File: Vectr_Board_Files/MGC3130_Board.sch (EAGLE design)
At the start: 108 parts, among them U101 MCP1755S, U102 MGC3130, U201 74HCT595BQ,115, U202 74HCT595BQ,115, U203 74HCT595BQ,115

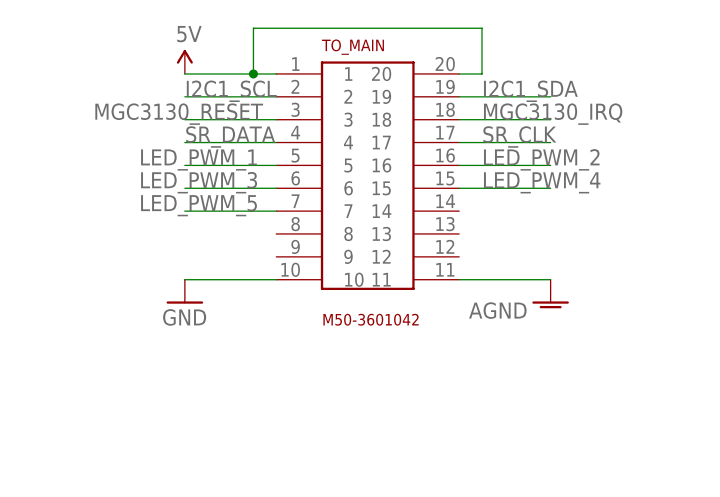
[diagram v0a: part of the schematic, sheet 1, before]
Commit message: Changing connectors
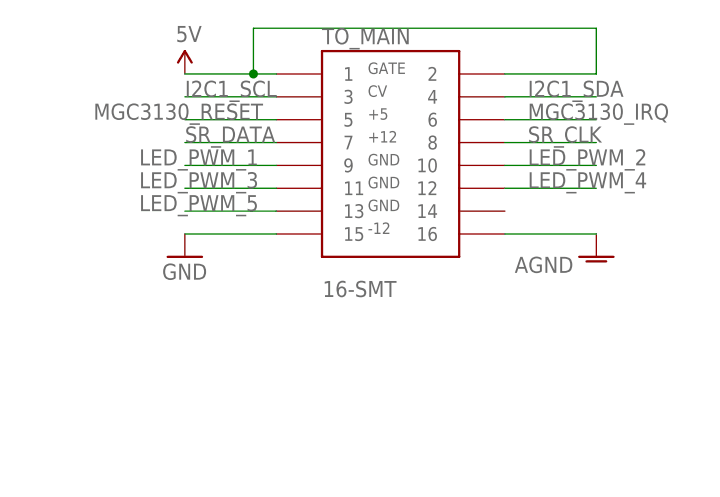
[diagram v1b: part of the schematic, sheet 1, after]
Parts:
- TO_MAIN: value M50-3601042 -> 16-SMT; device HackMe:M50-3601042 -> HackMe:16-SMT
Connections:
- net 5V: now also TO_MAIN.2; no longer TO_MAIN.20
- net AGND: now also TO_MAIN.16; no longer TO_MAIN.11
- net GND: now also TO_MAIN.15; no longer TO_MAIN.10
- net I2C1_SCL: now also TO_MAIN.3; no longer TO_MAIN.2
- net I2C1_SDA: now also TO_MAIN.4; no longer TO_MAIN.19
- net LED_PWM_1: now also TO_MAIN.9; no longer TO_MAIN.5
- net LED_PWM_2: now also TO_MAIN.10; no longer TO_MAIN.16
- net LED_PWM_3: now also TO_MAIN.11; no longer TO_MAIN.6
- net LED_PWM_4: now also TO_MAIN.12; no longer TO_MAIN.15
- net LED_PWM_5: now also TO_MAIN.13; no longer TO_MAIN.7
- net MGC3130_IRQ: now also TO_MAIN.6; no longer TO_MAIN.18
- net MGC3130_RESET: now also TO_MAIN.5; no longer TO_MAIN.3
- net SR_CLK: now also TO_MAIN.8; no longer TO_MAIN.17
- net SR_DATA: now also TO_MAIN.7; no longer TO_MAIN.4
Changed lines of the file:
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@@
 <part name="GND2" library="supply1" deviceset="GND" device=""/>
 <part name="AGND3" library="supply1" deviceset="AGND" device=""/>
-<part name="TO_MAIN" library="HackMe" deviceset="M50-3601042" device=""/>
 <part name="USB_BRIDGE" library="HackMe" deviceset="1X6_2MM_HEADER" device=""/>
+<part name="TO_MAIN" library="HackMe" deviceset="16-SMT" device=""/>
 </parts>
 <sheets>
@@
 <instance part="SUPPLY33" gate="G$1" x="-78.74" y="88.9"/>
 <instance part="SUPPLY38" gate="G$1" x="55.88" y="91.44"/>
-<instance part="GND34" gate="1" x="55.88" y="66.04"/>
-<instance part="AGND14" gate="VR1" x="96.52" y="66.04" smashed="yes">
-<attribute name="VALUE" x="93.98" y="66.04" size="1.778" layer="96" rot="R180"/>
+<instance part="GND34" gate="1" x="55.88" y="71.12"/>
+<instance part="AGND14" gate="VR1" x="101.6" y="71.12" smashed="yes">
+<attribute name="VALUE" x="99.06" y="71.12" size="1.778" layer="96" rot="R180"/>
 </instance>
 <instance part="AGND17" gate="VR1" x="-7.62" y="-45.72" smashed="yes">
@@
 <attribute name="VALUE" x="20.32" y="-20.32" size="1.778" layer="96" rot="R180"/>
 </instance>
-<instance part="TO_MAIN" gate="G$1" x="73.66" y="76.2"/>
 <instance part="USB_BRIDGE" gate="G$1" x="-71.12" y="-73.66"/>
+<instance part="TO_MAIN" gate="G$1" x="76.2" y="83.82"/>
 </instances>
 <busses>
@@
 <segment>
 <pinref part="GND34" gate="1" pin="GND"/>
-<wire x1="66.04" y1="68.58" x2="55.88" y2="68.58" width="0.1524" layer="91"/>
-<pinref part="TO_MAIN" gate="G$1" pin="10"/>
+<wire x1="66.04" y1="73.66" x2="55.88" y2="73.66" width="0.1524" layer="91"/>
+<pinref part="TO_MAIN" gate="G$1" pin="15"/>
 </segment>
 <segment>
@@
 </segment>
 <segment>
-<wire x1="86.36" y1="86.36" x2="96.52" y2="86.36" width="0.1524" layer="91"/>
-<label x="88.9" y="86.36" size="1.778" layer="95"/>
-<pinref part="TO_MAIN" gate="G$1" pin="18"/>
+<wire x1="91.44" y1="86.36" x2="101.6" y2="86.36" width="0.1524" layer="91"/>
+<label x="93.98" y="86.36" size="1.778" layer="95"/>
+<pinref part="TO_MAIN" gate="G$1" pin="6"/>
 </segment>
 <segment>
@@
 </segment>
 <segment>
-<wire x1="86.36" y1="88.9" x2="96.52" y2="88.9" width="0.1524" layer="91"/>
-<label x="88.9" y="88.9" size="1.778" layer="95"/>
-<pinref part="TO_MAIN" gate="G$1" pin="19"/>
+<wire x1="91.44" y1="88.9" x2="101.6" y2="88.9" width="0.1524" layer="91"/>
+<label x="93.98" y="88.9" size="1.778" layer="95"/>
+<pinref part="TO_MAIN" gate="G$1" pin="4"/>
 </segment>
 <segment>
@@
 <wire x1="66.04" y1="88.9" x2="55.88" y2="88.9" width="0.1524" layer="91"/>
 <label x="55.88" y="88.9" size="1.778" layer="95"/>
-<pinref part="TO_MAIN" gate="G$1" pin="2"/>
+<pinref part="TO_MAIN" gate="G$1" pin="3"/>
 </segment>
 <segment>
@@
 <wire x1="66.04" y1="86.36" x2="55.88" y2="86.36" width="0.1524" layer="91"/>
 <label x="45.72" y="86.36" size="1.778" layer="95"/>
-<pinref part="TO_MAIN" gate="G$1" pin="3"/>
+<pinref part="TO_MAIN" gate="G$1" pin="5"/>
 </segment>
 <segment>
@@
 <wire x1="63.5" y1="91.44" x2="63.5" y2="96.52" width="0.1524" layer="91"/>
 <junction x="63.5" y="91.44"/>
-<wire x1="63.5" y1="96.52" x2="88.9" y2="96.52" width="0.1524" layer="91"/>
-<wire x1="88.9" y1="96.52" x2="88.9" y2="91.44" width="0.1524" layer="91"/>
-<wire x1="88.9" y1="91.44" x2="86.36" y2="91.44" width="0.1524" layer="91"/>
+<wire x1="63.5" y1="96.52" x2="101.6" y2="96.52" width="0.1524" layer="91"/>
+<wire x1="101.6" y1="96.52" x2="101.6" y2="91.44" width="0.1524" layer="91"/>
+<wire x1="101.6" y1="91.44" x2="91.44" y2="91.44" width="0.1524" layer="91"/>
 <pinref part="TO_MAIN" gate="G$1" pin="1"/>
-<pinref part="TO_MAIN" gate="G$1" pin="20"/>
+<pinref part="TO_MAIN" gate="G$1" pin="2"/>
 </segment>
 </net>
@@
 <segment>
 <pinref part="AGND14" gate="VR1" pin="AGND"/>
-<wire x1="86.36" y1="68.58" x2="96.52" y2="68.58" width="0.1524" layer="91"/>
-<pinref part="TO_MAIN" gate="G$1" pin="11"/>
+<wire x1="91.44" y1="73.66" x2="101.6" y2="73.66" width="0.1524" layer="91"/>
+<pinref part="TO_MAIN" gate="G$1" pin="16"/>
 </segment>
 <segment>
@@
 <wire x1="66.04" y1="83.82" x2="55.88" y2="83.82" width="0.1524" layer="91"/>
 <label x="55.88" y="83.82" size="1.778" layer="95"/>
-<pinref part="TO_MAIN" gate="G$1" pin="4"/>
+<pinref part="TO_MAIN" gate="G$1" pin="7"/>
 </segment>
 </net>
 <net name="SR_CLK" class="0">
 <segment>
-<wire x1="86.36" y1="83.82" x2="96.52" y2="83.82" width="0.1524" layer="91"/>
-<label x="88.9" y="83.82" size="1.778" layer="95"/>
-<pinref part="TO_MAIN" gate="G$1" pin="17"/>
+<wire x1="91.44" y1="83.82" x2="101.6" y2="83.82" width="0.1524" layer="91"/>
+<label x="93.98" y="83.82" size="1.778" layer="95"/>
+<pinref part="TO_MAIN" gate="G$1" pin="8"/>
 </segment>
 </net>
@@
 <wire x1="66.04" y1="81.28" x2="55.88" y2="81.28" width="0.1524" layer="91"/>
 <label x="50.8" y="81.28" size="1.778" layer="95"/>
-<pinref part="TO_MAIN" gate="G$1" pin="5"/>
+<pinref part="TO_MAIN" gate="G$1" pin="9"/>
 </segment>
 </net>
 <net name="LED_PWM_2" class="0">
 <segment>
-<wire x1="86.36" y1="81.28" x2="96.52" y2="81.28" width="0.1524" layer="91"/>
-<label x="88.9" y="81.28" size="1.778" layer="95"/>
-<pinref part="TO_MAIN" gate="G$1" pin="16"/>
+<wire x1="91.44" y1="81.28" x2="101.6" y2="81.28" width="0.1524" layer="91"/>
+<label x="93.98" y="81.28" size="1.778" layer="95"/>
+<pinref part="TO_MAIN" gate="G$1" pin="10"/>
 </segment>
 </net>
@@
 <wire x1="66.04" y1="78.74" x2="55.88" y2="78.74" width="0.1524" layer="91"/>
 <label x="50.8" y="78.74" size="1.778" layer="95"/>
-<pinref part="TO_MAIN" gate="G$1" pin="6"/>
+<pinref part="TO_MAIN" gate="G$1" pin="11"/>
 </segment>
 </net>
 <net name="LED_PWM_4" class="0">
 <segment>
-<wire x1="86.36" y1="78.74" x2="96.52" y2="78.74" width="0.1524" layer="91"/>
-<label x="88.9" y="78.74" size="1.778" layer="95"/>
-<pinref part="TO_MAIN" gate="G$1" pin="15"/>
+<wire x1="91.44" y1="78.74" x2="101.6" y2="78.74" width="0.1524" layer="91"/>
+<label x="93.98" y="78.74" size="1.778" layer="95"/>
+<pinref part="TO_MAIN" gate="G$1" pin="12"/>
 </segment>
 </net>
@@
 <wire x1="66.04" y1="76.2" x2="55.88" y2="76.2" width="0.1524" layer="91"/>
 <label x="50.8" y="76.2" size="1.778" layer="95"/>
-<pinref part="TO_MAIN" gate="G$1" pin="7"/>
-</segment>
-</net>
+<pinref part="TO_MAIN" gate="G$1" pin="13"/>
+</segment>
+</net>

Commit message: Correcting the board files to match original production Vectr
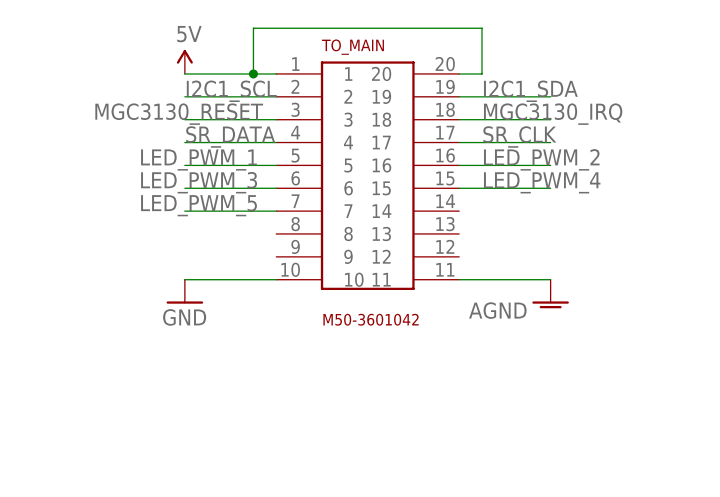
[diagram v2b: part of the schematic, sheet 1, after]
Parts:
- TO_MAIN: value 16-SMT -> M50-3601042; device HackMe:16-SMT -> HackMe:M50-3601042
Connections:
- net 5V: now also TO_MAIN.20; no longer TO_MAIN.2
- net AGND: now also TO_MAIN.11; no longer TO_MAIN.16
- net GND: now also TO_MAIN.10; no longer TO_MAIN.15
- net I2C1_SCL: now also TO_MAIN.2; no longer TO_MAIN.3
- net I2C1_SDA: now also TO_MAIN.19; no longer TO_MAIN.4
- net LED_PWM_1: now also TO_MAIN.5; no longer TO_MAIN.9
- net LED_PWM_2: now also TO_MAIN.16; no longer TO_MAIN.10
- net LED_PWM_3: now also TO_MAIN.6; no longer TO_MAIN.11
- net LED_PWM_4: now also TO_MAIN.15; no longer TO_MAIN.12
- net LED_PWM_5: now also TO_MAIN.7; no longer TO_MAIN.13
- net MGC3130_IRQ: now also TO_MAIN.18; no longer TO_MAIN.6
- net MGC3130_RESET: now also TO_MAIN.3; no longer TO_MAIN.5
- net SR_CLK: now also TO_MAIN.17; no longer TO_MAIN.8
- net SR_DATA: now also TO_MAIN.4; no longer TO_MAIN.7
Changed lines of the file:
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@@
 <part name="GND2" library="supply1" deviceset="GND" device=""/>
 <part name="AGND3" library="supply1" deviceset="AGND" device=""/>
+<part name="TO_MAIN" library="HackMe" deviceset="M50-3601042" device=""/>
 <part name="USB_BRIDGE" library="HackMe" deviceset="1X6_2MM_HEADER" device=""/>
-<part name="TO_MAIN" library="HackMe" deviceset="16-SMT" device=""/>
 </parts>
 <sheets>
@@
 <instance part="SUPPLY33" gate="G$1" x="-78.74" y="88.9"/>
 <instance part="SUPPLY38" gate="G$1" x="55.88" y="91.44"/>
-<instance part="GND34" gate="1" x="55.88" y="71.12"/>
-<instance part="AGND14" gate="VR1" x="101.6" y="71.12" smashed="yes">
-<attribute name="VALUE" x="99.06" y="71.12" size="1.778" layer="96" rot="R180"/>
+<instance part="GND34" gate="1" x="55.88" y="66.04"/>
+<instance part="AGND14" gate="VR1" x="96.52" y="66.04" smashed="yes">
+<attribute name="VALUE" x="93.98" y="66.04" size="1.778" layer="96" rot="R180"/>
 </instance>
 <instance part="AGND17" gate="VR1" x="-7.62" y="-45.72" smashed="yes">
@@
 <attribute name="VALUE" x="20.32" y="-20.32" size="1.778" layer="96" rot="R180"/>
 </instance>
+<instance part="TO_MAIN" gate="G$1" x="73.66" y="76.2"/>
 <instance part="USB_BRIDGE" gate="G$1" x="-71.12" y="-73.66"/>
-<instance part="TO_MAIN" gate="G$1" x="76.2" y="83.82"/>
 </instances>
 <busses>
@@
 <segment>
 <pinref part="GND34" gate="1" pin="GND"/>
-<wire x1="66.04" y1="73.66" x2="55.88" y2="73.66" width="0.1524" layer="91"/>
-<pinref part="TO_MAIN" gate="G$1" pin="15"/>
+<wire x1="66.04" y1="68.58" x2="55.88" y2="68.58" width="0.1524" layer="91"/>
+<pinref part="TO_MAIN" gate="G$1" pin="10"/>
 </segment>
 <segment>
@@
 </segment>
 <segment>
-<wire x1="91.44" y1="86.36" x2="101.6" y2="86.36" width="0.1524" layer="91"/>
-<label x="93.98" y="86.36" size="1.778" layer="95"/>
-<pinref part="TO_MAIN" gate="G$1" pin="6"/>
+<wire x1="86.36" y1="86.36" x2="96.52" y2="86.36" width="0.1524" layer="91"/>
+<label x="88.9" y="86.36" size="1.778" layer="95"/>
+<pinref part="TO_MAIN" gate="G$1" pin="18"/>
 </segment>
 <segment>
@@
 </segment>
 <segment>
-<wire x1="91.44" y1="88.9" x2="101.6" y2="88.9" width="0.1524" layer="91"/>
-<label x="93.98" y="88.9" size="1.778" layer="95"/>
-<pinref part="TO_MAIN" gate="G$1" pin="4"/>
+<wire x1="86.36" y1="88.9" x2="96.52" y2="88.9" width="0.1524" layer="91"/>
+<label x="88.9" y="88.9" size="1.778" layer="95"/>
+<pinref part="TO_MAIN" gate="G$1" pin="19"/>
 </segment>
 <segment>
@@
 <wire x1="66.04" y1="88.9" x2="55.88" y2="88.9" width="0.1524" layer="91"/>
 <label x="55.88" y="88.9" size="1.778" layer="95"/>
-<pinref part="TO_MAIN" gate="G$1" pin="3"/>
+<pinref part="TO_MAIN" gate="G$1" pin="2"/>
 </segment>
 <segment>
@@
 <wire x1="66.04" y1="86.36" x2="55.88" y2="86.36" width="0.1524" layer="91"/>
 <label x="45.72" y="86.36" size="1.778" layer="95"/>
-<pinref part="TO_MAIN" gate="G$1" pin="5"/>
+<pinref part="TO_MAIN" gate="G$1" pin="3"/>
 </segment>
 <segment>
@@
 <wire x1="63.5" y1="91.44" x2="63.5" y2="96.52" width="0.1524" layer="91"/>
 <junction x="63.5" y="91.44"/>
-<wire x1="63.5" y1="96.52" x2="101.6" y2="96.52" width="0.1524" layer="91"/>
-<wire x1="101.6" y1="96.52" x2="101.6" y2="91.44" width="0.1524" layer="91"/>
-<wire x1="101.6" y1="91.44" x2="91.44" y2="91.44" width="0.1524" layer="91"/>
+<wire x1="63.5" y1="96.52" x2="88.9" y2="96.52" width="0.1524" layer="91"/>
+<wire x1="88.9" y1="96.52" x2="88.9" y2="91.44" width="0.1524" layer="91"/>
+<wire x1="88.9" y1="91.44" x2="86.36" y2="91.44" width="0.1524" layer="91"/>
 <pinref part="TO_MAIN" gate="G$1" pin="1"/>
-<pinref part="TO_MAIN" gate="G$1" pin="2"/>
+<pinref part="TO_MAIN" gate="G$1" pin="20"/>
 </segment>
 </net>
@@
 <segment>
 <pinref part="AGND14" gate="VR1" pin="AGND"/>
-<wire x1="91.44" y1="73.66" x2="101.6" y2="73.66" width="0.1524" layer="91"/>
-<pinref part="TO_MAIN" gate="G$1" pin="16"/>
+<wire x1="86.36" y1="68.58" x2="96.52" y2="68.58" width="0.1524" layer="91"/>
+<pinref part="TO_MAIN" gate="G$1" pin="11"/>
 </segment>
 <segment>
@@
 <wire x1="66.04" y1="83.82" x2="55.88" y2="83.82" width="0.1524" layer="91"/>
 <label x="55.88" y="83.82" size="1.778" layer="95"/>
-<pinref part="TO_MAIN" gate="G$1" pin="7"/>
+<pinref part="TO_MAIN" gate="G$1" pin="4"/>
 </segment>
 </net>
 <net name="SR_CLK" class="0">
 <segment>
-<wire x1="91.44" y1="83.82" x2="101.6" y2="83.82" width="0.1524" layer="91"/>
-<label x="93.98" y="83.82" size="1.778" layer="95"/>
-<pinref part="TO_MAIN" gate="G$1" pin="8"/>
+<wire x1="86.36" y1="83.82" x2="96.52" y2="83.82" width="0.1524" layer="91"/>
+<label x="88.9" y="83.82" size="1.778" layer="95"/>
+<pinref part="TO_MAIN" gate="G$1" pin="17"/>
 </segment>
 </net>
@@
 <wire x1="66.04" y1="81.28" x2="55.88" y2="81.28" width="0.1524" layer="91"/>
 <label x="50.8" y="81.28" size="1.778" layer="95"/>
-<pinref part="TO_MAIN" gate="G$1" pin="9"/>
+<pinref part="TO_MAIN" gate="G$1" pin="5"/>
 </segment>
 </net>
 <net name="LED_PWM_2" class="0">
 <segment>
-<wire x1="91.44" y1="81.28" x2="101.6" y2="81.28" width="0.1524" layer="91"/>
-<label x="93.98" y="81.28" size="1.778" layer="95"/>
-<pinref part="TO_MAIN" gate="G$1" pin="10"/>
+<wire x1="86.36" y1="81.28" x2="96.52" y2="81.28" width="0.1524" layer="91"/>
+<label x="88.9" y="81.28" size="1.778" layer="95"/>
+<pinref part="TO_MAIN" gate="G$1" pin="16"/>
 </segment>
 </net>
@@
 <wire x1="66.04" y1="78.74" x2="55.88" y2="78.74" width="0.1524" layer="91"/>
 <label x="50.8" y="78.74" size="1.778" layer="95"/>
-<pinref part="TO_MAIN" gate="G$1" pin="11"/>
+<pinref part="TO_MAIN" gate="G$1" pin="6"/>
 </segment>
 </net>
 <net name="LED_PWM_4" class="0">
 <segment>
-<wire x1="91.44" y1="78.74" x2="101.6" y2="78.74" width="0.1524" layer="91"/>
-<label x="93.98" y="78.74" size="1.778" layer="95"/>
-<pinref part="TO_MAIN" gate="G$1" pin="12"/>
+<wire x1="86.36" y1="78.74" x2="96.52" y2="78.74" width="0.1524" layer="91"/>
+<label x="88.9" y="78.74" size="1.778" layer="95"/>
+<pinref part="TO_MAIN" gate="G$1" pin="15"/>
 </segment>
 </net>
@@
 <wire x1="66.04" y1="76.2" x2="55.88" y2="76.2" width="0.1524" layer="91"/>
 <label x="50.8" y="76.2" size="1.778" layer="95"/>
-<pinref part="TO_MAIN" gate="G$1" pin="13"/>
-</segment>
-</net>
+<pinref part="TO_MAIN" gate="G$1" pin="7"/>
+</segment>
+</net>
